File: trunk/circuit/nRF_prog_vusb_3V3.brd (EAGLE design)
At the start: 50 x 50 mm, 26 parts, among them Q2 12MHz

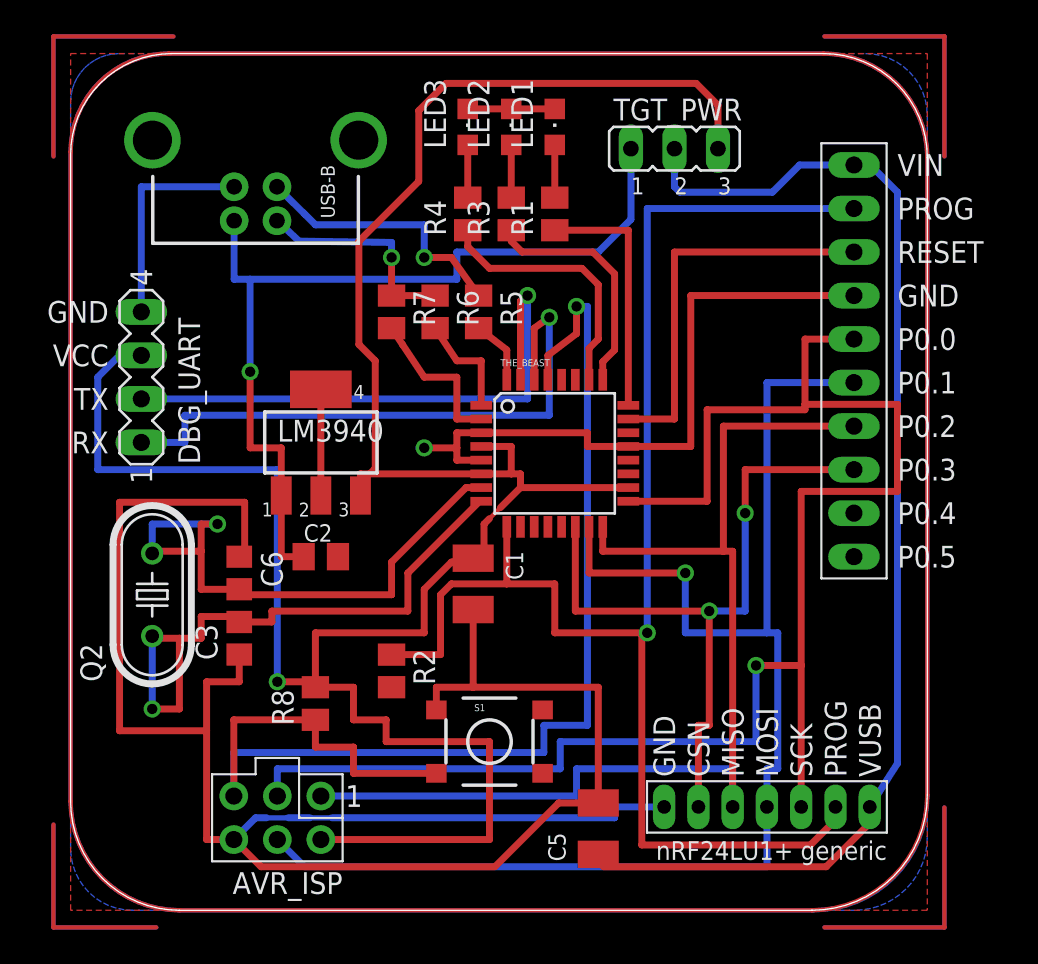
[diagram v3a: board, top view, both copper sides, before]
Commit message: 
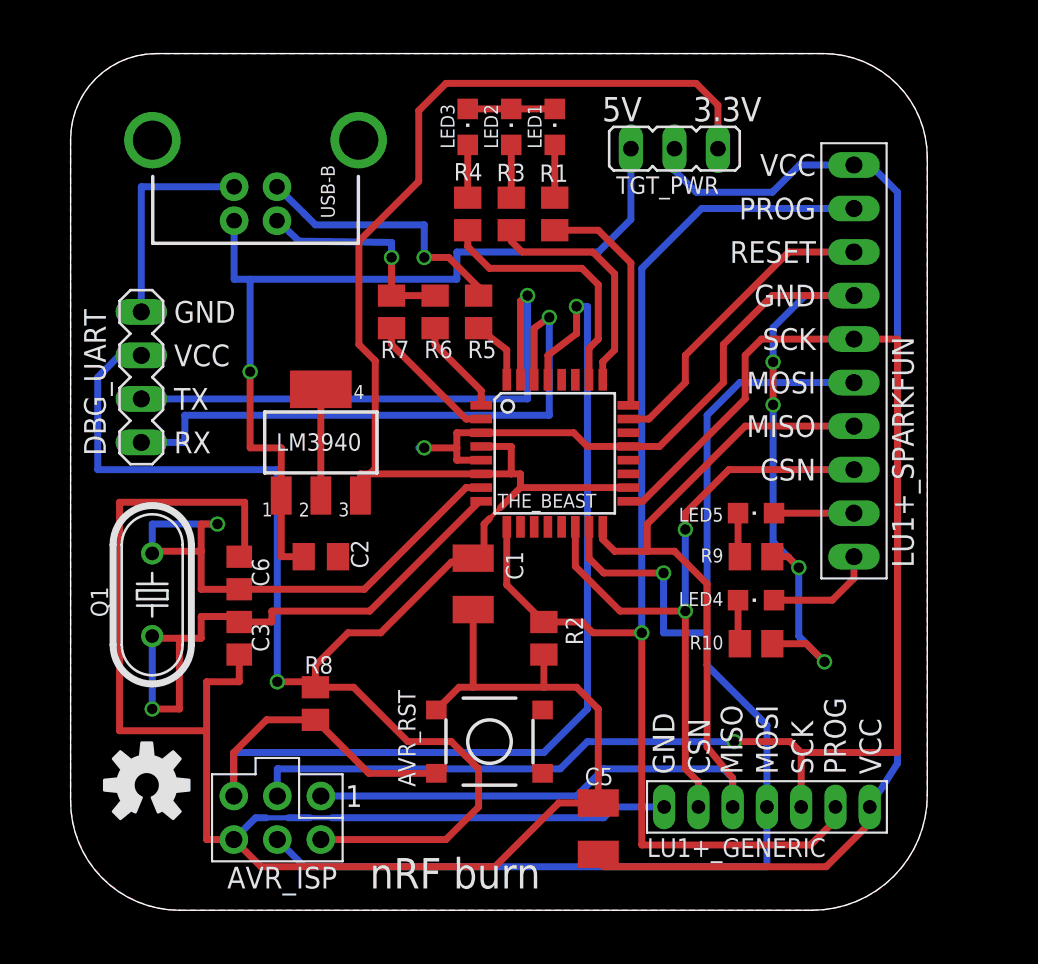
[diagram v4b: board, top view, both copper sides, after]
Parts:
- added LED4, LED5: (no value), led:CHIPLED_0805
- added R10, R9: 1K, rcl:M0805
- added U$1: OSHW-LOGOM, SparkFun:OSHW-LOGO-M
- TGT_PWR: device jumper:JP2 -> KileParts:JP2
- moved R2 9.09 mm to (27.6, 15.9)
- renumbered NRF_GEN to LU1+_GENERIC, Q2 to Q1, S1 to AVR_RST, U$2 to LU1+_SPARKFUN
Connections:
- new net N$1: LED4.A, LU1+_SPARKFUN.P0.5
- new net N$2: LED5.A, LU1+_SPARKFUN.P0.4
- new net N$3: LED4.C, R10.2
- new net N$4: LED5.C, R9.2
- net GND: now also R10.1, R9.1
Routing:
- net N$2: track 185.5 -> 4.66 mm
- net N$1: track 185.4 -> 6.46 mm
- net GND: track 177.3 -> 204.6 mm, vias 1 -> 5
- net PROG: track 87.1 -> 72.6 mm
- net N$7: track 14.0 -> 0.00 mm
- net N$12: track 14.0 -> 0.00 mm
- net N$11: track 14.0 -> 0.00 mm
- net N$10: track 14.0 -> 0.00 mm
- net N$6: track 12.0 -> 0.00 mm
- net N$5: track 12.0 -> 0.00 mm
- net N$4: track 14.0 -> 2.58 mm
- net N$3: track 14.0 -> 2.58 mm
- net P0.0: track 95.3 -> 87.1 mm
- net 3.3V: track 149.2 -> 141.4 mm
- net TGT_RST: track 22.9 -> 18.1 mm
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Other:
- outline, holes or cut-outs redrawn
- board text added: "3.3V"
- board text added: "5V"
- board text added: "CSN"
- board text added: "GND"
- board text added: "MISO"
- board text added: "MOSI"
- board text added: "PROG"
- board text added: "RESET"
- board text added: "SCK"
- board text added: "VCC"
- board text added: "nRF burn"

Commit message: 
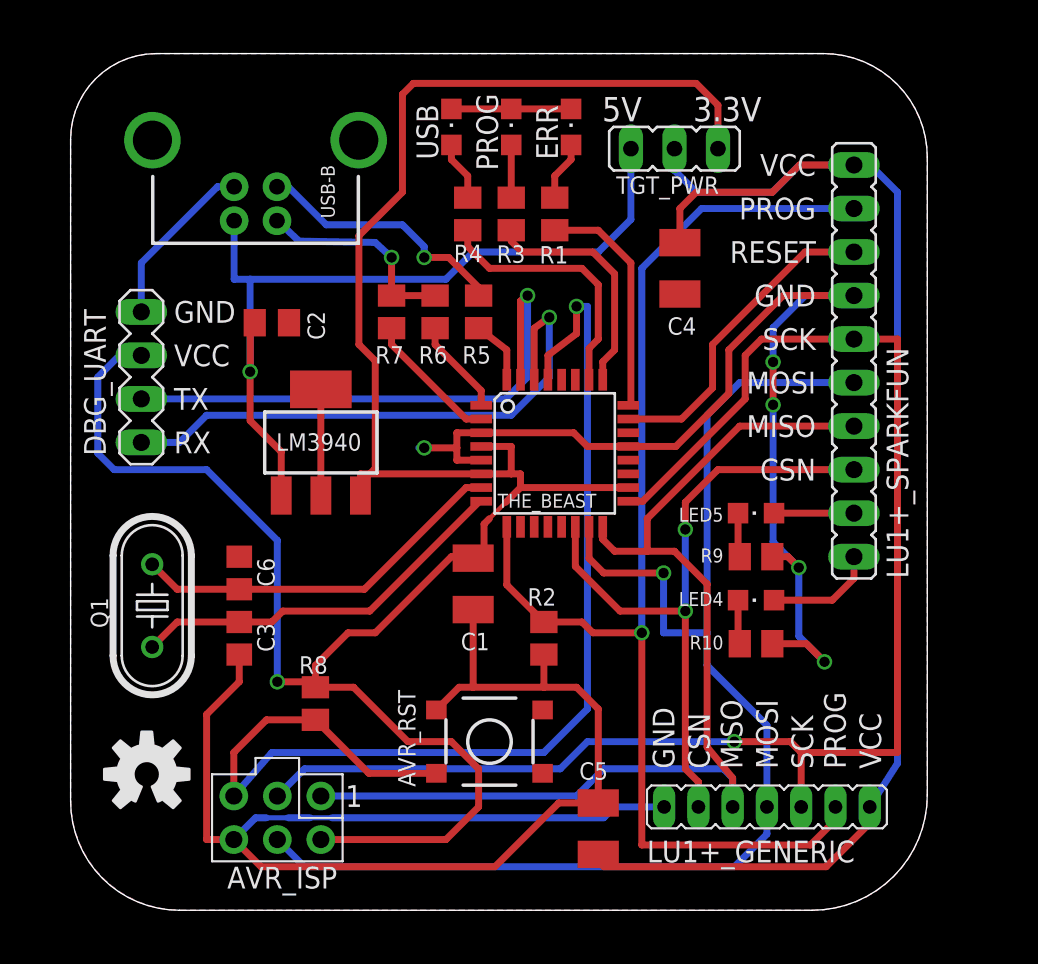
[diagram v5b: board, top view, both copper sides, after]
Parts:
- removed LED1, LED3: (no value), led:CHIPLED_0805
- added C4: 10uF, rcl:SMC_B
- added ERR, USB: (no value), led:CHIPLED_0805
- added U$2: OSHW-LOGOL, SparkFun:OSHW-LOGO-L
- moved C2 13.9 mm to (11.7, 34.3)
- moved LU1+_SPARKFUN 7.73 mm to (45.7, 32.1)
- moved U$1 0.63 mm to (4.45, 7.94)
- moved Q1 0.63 mm to (4.76, 17.8)
- renumbered LED2 to PROG
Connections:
- net GND: now also C4.-, ERR.C, USB.C; no longer LED1.C, LED3.C
- net N$18: now also USB.A; no longer LED3.A
- net N$20: now also ERR.A; no longer LED1.A
- net VIN: now also C4.+
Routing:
- net GND: track 204.6 -> 174.0 mm
- net VIN: track 71.0 -> 84.3 mm
- net N$27: track 34.1 -> 22.7 mm, vias 1 -> 0
- net N$26: track 32.3 -> 22.3 mm, vias 1 -> 0
- net VBUS: track 52.4 -> 48.5 mm
- net RX: track 35.2 -> 33.0 mm
- net 3.3V: track 141.4 -> 139.7 mm
- net AVR_RESET: track 69.9 -> 68.5 mm
- net P0.1: track 79.0 -> 77.8 mm
- net P0.0: track 87.1 -> 86.2 mm
- net TX: track 33.7 -> 32.9 mm
- net USB_D+: track 15.8 -> 15.1 mm
- net TGT_RST: track 18.1 -> 18.7 mm
- net USB_D-: track 12.8 -> 12.3 mm
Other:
- board text added: "nRF Burner v1.0"
- board text added: "source code, circuit and PCB: https://code.google.com/p/nrfburn/"
- board text removed: "nRF burn"

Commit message: 
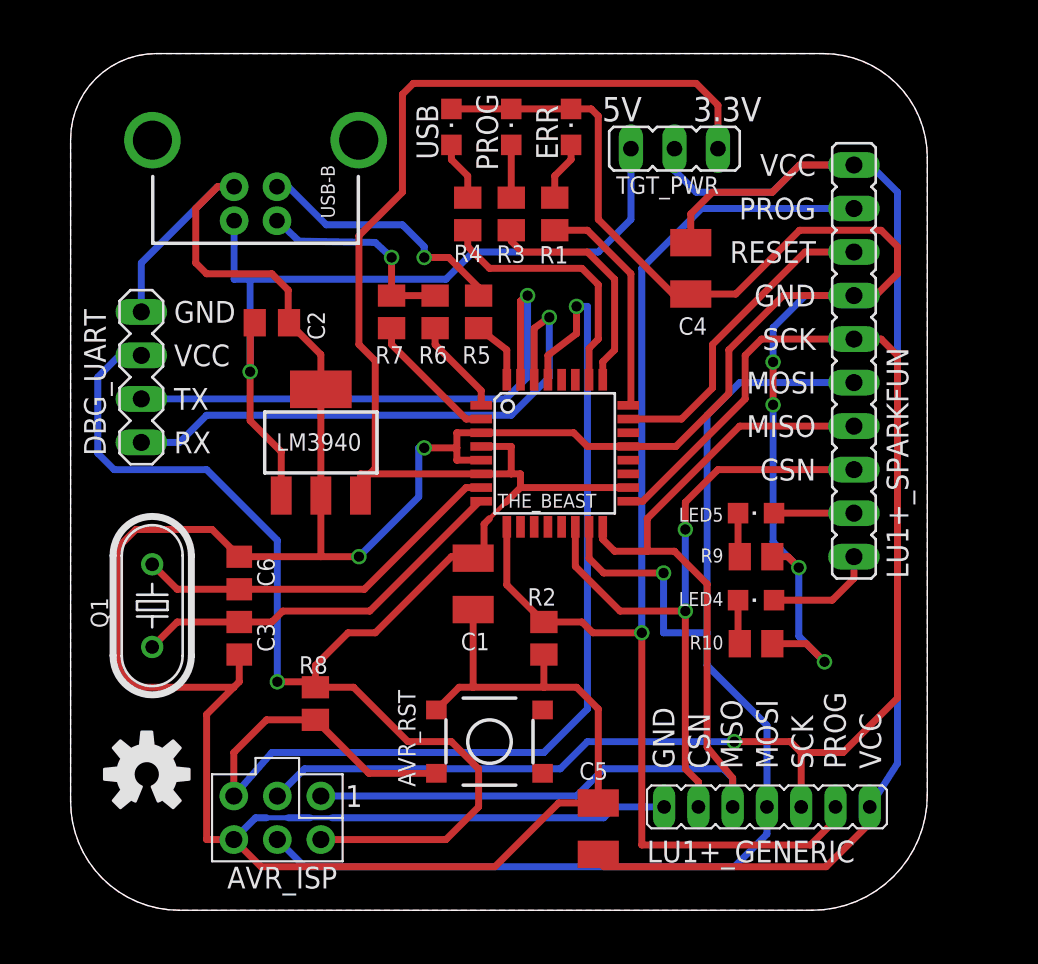
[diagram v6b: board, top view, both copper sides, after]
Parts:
- moved C4 0.63 mm to (36.2, 37.5)
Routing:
- net GND: track 174.0 -> 266.8 mm, vias 5 -> 6
- net P0.0: track 86.2 -> 83.8 mm
- net VIN: track 84.3 -> 83.4 mm

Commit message: added testpins for USB
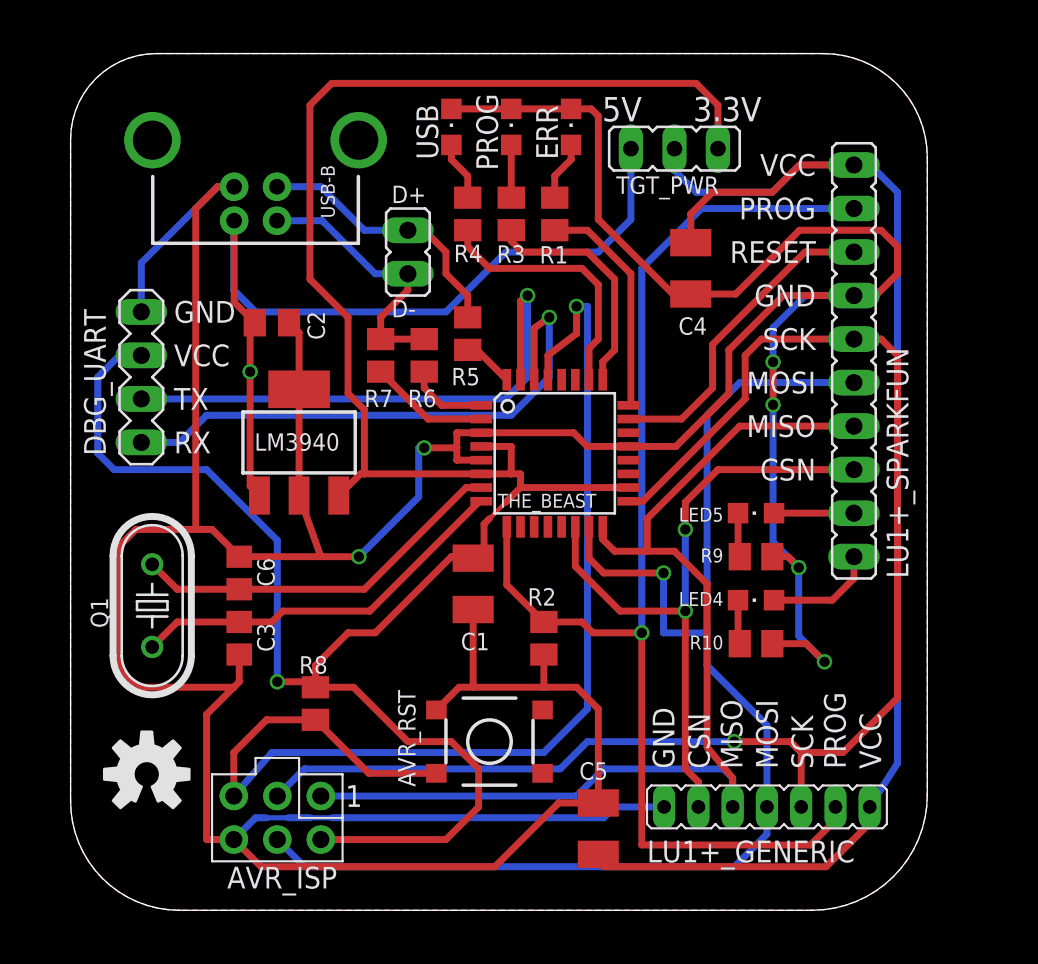
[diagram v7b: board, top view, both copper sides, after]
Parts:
- added JP1: (no value), KileParts:JP1
- moved R6 2.62 mm to (20.6, 32.4)
- moved R7 2.62 mm to (18.1, 32.4)
- moved R5 1.42 mm to (23.2, 33.7)
- moved LM3940 1.27 mm to (13.3, 27.3)
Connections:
- net USB_D+: now also JP1.2
- net USB_D-: now also JP1.1
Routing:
- net GND: track 266.8 -> 274.2 mm
- net 3.3V: track 139.7 -> 144.9 mm
- net USB_D-: track 12.3 -> 15.9 mm, vias 1 -> 0
- net VBUS: track 48.5 -> 51.0 mm
- net DPULLUP: track 7.99 -> 7.01 mm
- net D-: track 5.62 -> 4.70 mm
- net D+: track 3.82 -> 3.00 mm
- net USB_D+: track 15.1 -> 15.8 mm, vias 1 -> 0
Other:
- board text added: "D+"
- board text added: "D-"
